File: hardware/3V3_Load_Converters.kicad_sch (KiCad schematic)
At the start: 78 parts, among them J23 61300311121, J24 61300311121, Q28 EPC2016C, Q29 EPC2016C, Q30 EPC2016C, Q31 EPC2016C, Q8 SI2302DDS-T1-GE3, Q9 SI2302DDS-T1-GE3, U21 INA199C3DCKR, U30 LTC3833EUDC-TRPBF, U31 LTC3833EUDC-TRPBF

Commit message: hardware: Making improvements for first release
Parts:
- C10, C11, C20, C21, C3: MPN (none) -> C0603C104K5RACTU; Manufacturer (none) -> KEMET; Package (none) -> SMD 0603; automotive Yes -> (none); automotive grade Grade 1 -> (none); capacitance 0.10 μF -> (none); category Cap -> (none); device class L1 Passive Components -> (none); device class L2 Capacitors -> (none); device class L3 Ceramic Capacitors -> (none); digikey description CAP CER 0.1UF 50V X7R 0603 -> (none); digikey part number 399-5089-2-ND -> (none); height 0.87mm -> (none); lead free Yes -> (none); library id 73022d3323b2b2b8 -> (none); manufacturer KEMET -> (none); material Ceramic -> (none); mouser part number 80-C0603C104K5R7867 -> (none); package 0603 -> (none); rohs Yes -> (none); temperature characteristic X7R -> (none); temperature coefficient 30ppm/°C -> (none); temperature range high +125°C -> (none); temperature range low -55°C -> (none); tolerance 0.1 -> (none); voltage rating 50 V -> (none)
- C12, C13: MPN (none) -> C0603C332J5GACAUTO; Manufacturer (none) -> KEMET; Package (none) -> SMD 0603; automotive Yes -> (none); automotive grade Grade 1 -> (none); capacitance 3,300 pF -> (none); category Cap -> (none); device class L1 Passive Components -> (none); device class L2 Capacitors -> (none); device class L3 Ceramic Capacitors -> (none); digikey description CAP CER 3300PF 50V C0G/NP0 0603 -> (none); digikey part number 399-16013-2-ND -> (none); height 0.87mm -> (none); lead free Yes -> (none); library id bd73e4c017624772 -> (none); manufacturer KEMET -> (none); material Ceramic -> (none); mouser description Cap Ceramic 0.0033uF 50V C0G 5% Pad SMD 0603 125C Automotiv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 -> (none); mouser part number 80-C0603C332J5GAUTO -> (none); package 0603 -> (none); rohs Yes -> (none); temperature characteristic C0G -> (none); temperature coefficient 30ppm/°C -> (none); temperature range high +125°C -> (none); temperature range low -55°C -> (none); tolerance 0.05 -> (none); voltage rating 50 V -> (none)
- C14, C15: MPN (none) -> C0603C101J5GACAUTO; Manufacturer (none) -> KEMET; Package (none) -> SMD 0603; automotive Yes -> (none); automotive grade Grade 1 -> (none); capacitance 100 pF -> (none); category Cap -> (none); device class L1 Passive Components -> (none); device class L2 Capacitors -> (none); device class L3 Ceramic Capacitors -> (none); digikey description CAP CER 100PF 50V C0G/NP0 0603 -> (none); digikey part number 399-6842-2-ND -> (none); height 0.87mm -> (none); lead free Yes -> (none); library id 9466b08f233088f0 -> (none); manufacturer KEMET -> (none); material Ceramic -> (none); mouser description Multilayer Ceramic Capacitors MLCC - SMD/SMT 100pF 50volts 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 -> (none); mouser part number 80-C0603C101J5GAUTO -> (none); package 0603 -> (none); rohs Yes -> (none); temperature characteristic C0G -> (none); temperature coefficient 30ppm/°C -> (none); temperature range high +125°C -> (none); temperature range low -55°C -> (none); tolerance 0.05 -> (none); voltage rating 50 V -> (none)
- C16, C17, C18, C19: MPN (none) -> C0603C102F3GACTU; Manufacturer (none) -> KEMET; Package (none) -> SMD 0603; automotive Yes -> (none); automotive grade Grade 1 -> (none); capacitance 1,000 pF -> (none); category Cap -> (none); device class L1 Passive Components -> (none); device class L2 Capacitors -> (none); device class L3 Ceramic Capacitors -> (none); digikey description CAP CER 1000PF 25V 1% NP0 0603 -> (none); digikey part number C0603C102F3GACTU-ND -> (none); height 0.87mm -> (none); lead free Yes -> (none); library id 46f08c8db7ea7e1d -> (none); manufacturer KEMET -> (none); material Ceramic -> (none); mouser description Capacitor, Ceramic, 1Nf, 25Vdc, 1-% Tol, 1+% Tol, C0g-Tc Co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 -> (none); mouser part number 80-C0603C102F3G -> (none); package 0603 -> (none); rohs Yes -> (none); temperature characteristic C0G -> (none); temperature coefficient 30ppm/°C -> (none); temperature range high +125°C -> (none); temperature range low -55°C -> (none); tolerance 0.01 -> (none); voltage rating 25 V -> (none)
- C22, C23: MPN (none) -> GCM32ER71H475KA55L; Manufacturer (none) -> Murata Electronics; Package (none) -> SMD 1210; automotive Yes -> (none); automotive grade Grade 1 -> (none); capacitance 4.7uF -> (none); category Cap -> (none); device class L1 Passive Components -> (none); device class L2 Capacitors -> (none); device class L3 Ceramic Capacitors -> (none); height 2.7mm -> (none); ipc land pattern name CAPC320250X250 -> (none); lead free Yes -> (none); library id 6d88f107f3aa88d3 -> (none); manufacturer Murata -> (none); material Ceramic -> (none); package 1210 -> (none); rohs Yes -> (none); temperature characteristic X7R -> (none); temperature coefficient 15% -> (none); temperature range high +125°C -> (none); temperature range low -55°C -> (none); tolerance 10% -> (none); voltage rating 50V -> (none)
- C24, C25: MPN (none) -> T495X476K035ATE300; Manufacturer (none) -> KEMET; Package (none) -> SMD 2917; automotive No -> (none); capacitance 47uF -> (none); category Cap -> (none); device class L1 Passive Components -> (none); device class L2 Capacitors -> (none); device class L3 Tantalum Capacitors -> (none); digikey description CAP TANT 47UF 10% 35V 2917 -> (none); digikey part number 399-3905-1-ND -> (none); dissipation factor 8% -> (none); esr 300mΩ -> (none); height 4.3mm -> (none); lead free Yes -> (none); leakage current 16.5uA -> (none); library id 9f2f9997282f5b7d -> (none); life 2000Hours -> (none); manufacturer Kemet -> (none); material Tantalum -> (none); mouser description Tantalum Capacitors - Solid SMD 35volts 47uF 10% ESR=300mOh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 -> (none); mouser part number 80-T495X476K35ATE300 -> (none); package 2917 -> (none); ripple current 742mA -> (none); rohs Yes -> (none); standoff height 0mm -> (none); temperature range high +125°C -> (none); temperature range low -55°C -> (none); tolerance 10% -> (none); voltage rating 35V -> (none)
- C26, C27, C28, C29: MPN (none) -> C1210C106K5RACTU; Manufacturer (none) -> KEMET; Package (none) -> SMD 1210; automotive No -> (none); capacitance 10uF -> (none); category Cap -> (none); device class L1 Passive Components -> (none); device class L2 Capacitors -> (none); device class L3 Ceramic Capacitors -> (none); digikey description CAP CER 10UF 50V X7R 1210 -> (none); digikey part number 399-11629-1-ND -> (none); height 2.8mm -> (none); ipc land pattern name CAPC320250X250 -> (none); lead free Yes -> (none); library id 80b9cd679ce51e4b -> (none); manufacturer KEMET -> (none); material Ceramic -> (none); mouser description Multilayer Ceramic Capacitors MLCC - SMD/SMT 50volts 10uF 1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 -> (none); mouser part number 80-C1210C106K5R -> (none); package 1210 -> (none); rohs Yes -> (none); temperature characteristic X7R -> (none); temperature coefficient 15% -> (none); temperature range high +125°C -> (none); temperature range low -55°C -> (none); tolerance 10% -> (none); voltage rating 50V -> (none)
- C30, C31: MPN (none) -> C0805C105K5RACTU; Manufacturer (none) -> KEMET; Package (none) -> SMD 0805; capacitance 1uF -> (none); category Cap -> (none); device class L1 Passive Components -> (none); device class L2 Capacitors -> (none); device class L3 Ceramic Capacitors -> (none); digikey description CAP CER 1UF 50V X7R 0805 -> (none); digikey part number 399-7409-2-ND -> (none); height 1.4mm -> (none); ipc land pattern name CAPC200125X787 -> (none); lead free yes -> (none); library id ac83af3950e2a3c3 -> (none); manufacturer Kemet -> (none); material Ceramic -> (none); mouser description Multilayer Ceramic Capacitors MLCC - SMD/SMT 1uF 50 Volts 1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 -> (none); mouser part number 80-C0805C105K5R -> (none); package 0805 (2012 metric) -> (none); rohs yes -> (none); standoff height 0mm -> (none); temperature characteristic X7R -> (none); temperature range high +125°C -> (none); temperature range low -55°C -> (none); tolerance 10% -> (none); voltage rating 50V -> (none)
- C32, C33: MPN (none) -> C0603C220K5RACAUTO; Manufacturer (none) -> KEMET; Package (none) -> SMD 0603; automotive Yes -> (none); automotive grade Grade 1 -> (none); capacitance 22 pF -> (none); category Cap -> (none); device class L1 Passive Components -> (none); device class L2 Capacitors -> (none); device class L3 Ceramic Capacitors -> (none); digikey description Cap Ceramic 22pF 50V X7R 10% SMD 0603 125°C Punched Paper T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 -> (none); digikey part number 399-13715-2-ND -> (none); height 0.87mm -> (none); lead free Yes -> (none); library id f369d16140aeee74 -> (none); manufacturer KEMET -> (none); material Ceramic -> (none); mouser description Cap Ceramic 22pF 50V X7R 10% SMD 0603 125°C Punched Paper T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 -> (none); mouser part number 80-C0603C220K5RAUTO -> (none); package 0603 -> (none); rohs Yes -> (none); temperature characteristic X7R -> (none); temperature coefficient 30ppm/°C -> (none); temperature range high +125°C -> (none); temperature range low -55°C -> (none); tolerance 0.1 -> (none); voltage rating 50 V -> (none)
- C34, C35, C36, C37, C38, C39: MPN (none) -> GCM32ER71C226KE19L; Manufacturer (none) -> Murata; Package (none) -> SMD 1210; automotive Yes -> (none); automotive grade Grade 1 -> (none); capacitance 22uF -> (none); category Cap -> (none); device class L1 Passive Components -> (none); device class L2 Capacitors -> (none); device class L3 Ceramic Capacitors -> (none); digikey description Cap Ceramic 22pF 50V X7R 10% SMD 0603 125°C Punched Paper T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 -> (none); digikey part number 399-13715-2-ND -> (none); height 2.7mm -> (none); ipc land pattern name CAPC320250X250 -> (none); lead free Yes -> (none); library id c3f1d06b93fd8ef7 -> (none); manufacturer Murata -> (none); material Ceramic -> (none); mouser description Cap Ceramic 22pF 50V X7R 10% SMD 0603 125°C Punched Paper T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 -> (none); mouser part number 80-C0603C220K5RAUTO -> (none); package 1210 -> (none); rohs Yes -> (none); temperature characteristic X7R -> (none); temperature coefficient 15% -> (none); temperature range high +125°C -> (none); temperature range low -55°C -> (none); tolerance 10% -> (none); voltage rating 16V -> (none)
- JP1, JP2: value SolderJumper_2_Bridged -> N/A; MPN (none) -> N/A; Manufacturer (none) -> N/A; Package (none) -> N/A
- L2: MPN (none) -> 744325240; Manufacturer (none) -> Wurth Elektronik; Manufacturer_Name Wurth Elektronik -> (none); Manufacturer_Part_Number 744325240 -> (none); Mouser Part Number 710-744325240 -> (none); Mouser Price/Stock https://www.mouser.co.uk/ProductDetail/Wurth-Elektronik/744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 -> (none); Package (none) -> Non-standard
- Q28, Q29, Q30, Q31: MPN (none) -> EPC2016C; Manufacturer (none) -> EPC; Package (none) -> Die (specific to EPC2016C); automotive No -> (none); category Trans -> (none); continuous drain current 18A -> (none); depletion mode False -> (none); device class L1 Discrete Semiconductors -> (none); device class L2 Transistors -> (none); device class L3 MOSFETs -> (none); digikey description GANFET TRANS 100V 18A BUMPED DIE -> (none); digikey part number 917-1080-1-ND -> (none); drain to source breakdown voltage 100V -> (none); drain to source resistance 12mΩ -> (none); drain to source voltage 100V -> (none); gate to source voltage +6/-4V -> (none); height 0.815mm -> (none); input capacitace at vds 360pF @ 50V -> (none); lead free Yes -> (none); library id edc307fffab956cd -> (none); manufacturer EPC -> (none); max junction temp +150°C -> (none); number of N channels 1 -> (none); number of channels 1 -> (none); package SMT_2MM106_1MM632 -> (none); pulse drain current 75A -> (none); reverse recovery charge 0nC -> (none); rohs Yes -> (none); rthja max 69°C/W -> (none); standoff height 0.08mm -> (none); technology GaN -> (none); temperature range high +150°C -> (none); temperature range low -40°C -> (none); threshold vgs max 2.5V -> (none); threshold vgs min 0.8V -> (none); typ forward diode voltage 1.8V -> (none)
- Q8, Q9: Height 1.12 -> (none); MPN (none) -> SI2302DDS-T1-GE3; Manufacturer (none) -> Vishay; Manufacturer_Name Vishay -> (none); Manufacturer_Part_Number SI2302DDS-T1-GE3 -> (none); Mouser Part Number 78-SI2302DDS-T1-GE3 -> (none); Mouser Price/Stock https://www.mouser.co.uk/ProductDetail/Vishay-Semiconductor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 -> (none); Package (none) -> SOT-23-3
- R33, R34, R39: Arrow Part Number CRCW0603100KFKEAHP -> (none); Arrow Price/Stock https://www.arrow.com/en/products/crcw0603100kfkeahp/vishay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 -> (none); Height 0.55 -> (none); MPN (none) -> CRCW0603100KFKEAHP; Manufacturer (none) -> Vishay; Manufacturer_Name Vishay -> (none); Manufacturer_Part_Number CRCW0603100KFKEAHP -> (none); Mouser Part Number 71-CRCW0603100KFKEAH -> (none); Mouser Price/Stock https://www.mouser.co.uk/ProductDetail/Vishay-Dale/CRCW0603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 -> (none); Package (none) -> SMD 0603
- R37, R38: MPN (none) -> CRCW060312K0FKEAHP; Manufacturer (none) -> Vishay; Package (none) -> SMD 0603; automotive Yes -> (none); automotive grade Grade 0 -> (none); category Res -> (none); composition Thick Film -> (none); device class L1 Passive Components -> (none); device class L2 Resistors -> (none); device class L3 Chip SMD Resistors -> (none); height 0.55mm -> (none); ipc land pattern name RESC16085X45 -> (none); lead free Yes -> (none); library id e050c09dfdbc8558 -> (none); manufacturer Vishay -> (none); package 0603 -> (none); power 250mW -> (none); power rating 0.33W -> (none); resistance 12kΩ -> (none); rohs Yes -> (none); series CRCW-HP e3 -> (none); temperature coefficient 100ppm/°C -> (none); temperature range high +155°C -> (none); temperature range low -55°C -> (none); tolerance 1% -> (none); voltage rating 75V -> (none)
- R47: MPN (none) -> WSL20108L000FEA18; Manufacturer (none) -> Vishay; Package (none) -> SMD 2010
- R50, R54: MPN (none) -> CRCW060390K9FKEAHP; Manufacturer (none) -> Vishay; Package (none) -> SMD 0603; automotive Yes -> (none); automotive grade Grade 0 -> (none); category Res -> (none); composition Thick Film -> (none); device class L1 Passive Components -> (none); device class L2 Resistors -> (none); device class L3 Chip SMD Resistors -> (none); height 0.55mm -> (none); ipc land pattern name RESC16085X45 -> (none); lead free Yes -> (none); library id 12344a549d2950d0 -> (none); manufacturer Vishay -> (none); package 0603 -> (none); power 250mW -> (none); power rating 0.33W -> (none); resistance 90.9kΩ -> (none); rohs Yes -> (none); series CRCW-HP e3 -> (none); temperature coefficient 100ppm/°C -> (none); temperature range high +155°C -> (none); temperature range low -55°C -> (none); tolerance 1% -> (none); voltage rating 75V -> (none)
- R52, R56: MPN (none) -> CRCW060320K0FKEAHP; Manufacturer (none) -> Vishay; Package (none) -> SMD 0603; automotive Yes -> (none); automotive grade Grade 0 -> (none); category Res -> (none); composition Thick Film -> (none); device class L1 Passive Components -> (none); device class L2 Resistors -> (none); device class L3 Chip SMD Resistors -> (none); height 0.55mm -> (none); ipc land pattern name RESC16085X45 -> (none); lead free Yes -> (none); library id 6d0e00b833a89e4b -> (none); manufacturer Vishay -> (none); package 0603 -> (none); power 250mW -> (none); power rating 0.33W -> (none); resistance 20kΩ -> (none); rohs Yes -> (none); series CRCW-HP e3 -> (none); temperature coefficient 100ppm/°C -> (none); temperature range high +155°C -> (none); temperature range low -55°C -> (none); tolerance 1% -> (none); voltage rating 75V -> (none)
- R76: MPN (none) -> CRCW06030000Z0EAHP; Manufacturer (none) -> Vishay; Package (none) -> SMD 0603
- R97: MPN (none) -> CRCW060382K0FKEA; Manufacturer (none) -> Vishay; Package (none) -> SMD 0603
- TP5: value 3V3 -> Test point; MPN (none) -> N/A; Manufacturer (none) -> N/A; Package (none) -> N/A
- U21: footprint Package_TO_SOT_SMD:SOT-363_SC-70-6 -> footprints:INA199C3DCKR; symbol INA199C3DCKR:INA199xxDCK -> INA199C3DCKR:INA199C3DCKR; MPN (none) -> INA199C3DCKR; Manufacturer (none) -> TI; Package (none) -> SC70-6
- U30, U31: value LTC3833EUDC-TRPBF -> LTC3833EUDC#TRPBF; symbol LTC3833EUDC#TRPBF:LTC3833EUDC-TRPBF -> LTC3833EUDC#TRPBF:LTC3833EUDC#TRPBF; MPN (none) -> LTC3833EUDC#TRPBF; Manufacturer (none) -> Analog Devices; Package (none) -> QFN-20
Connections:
- net AMUX7: no longer U21.6 (OUT)
- net GNDPWR: no longer U21.1 (REF)
- net VBUS_BK3V3: no longer U21.5 (IN-)
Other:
- moved on the sheet: U21

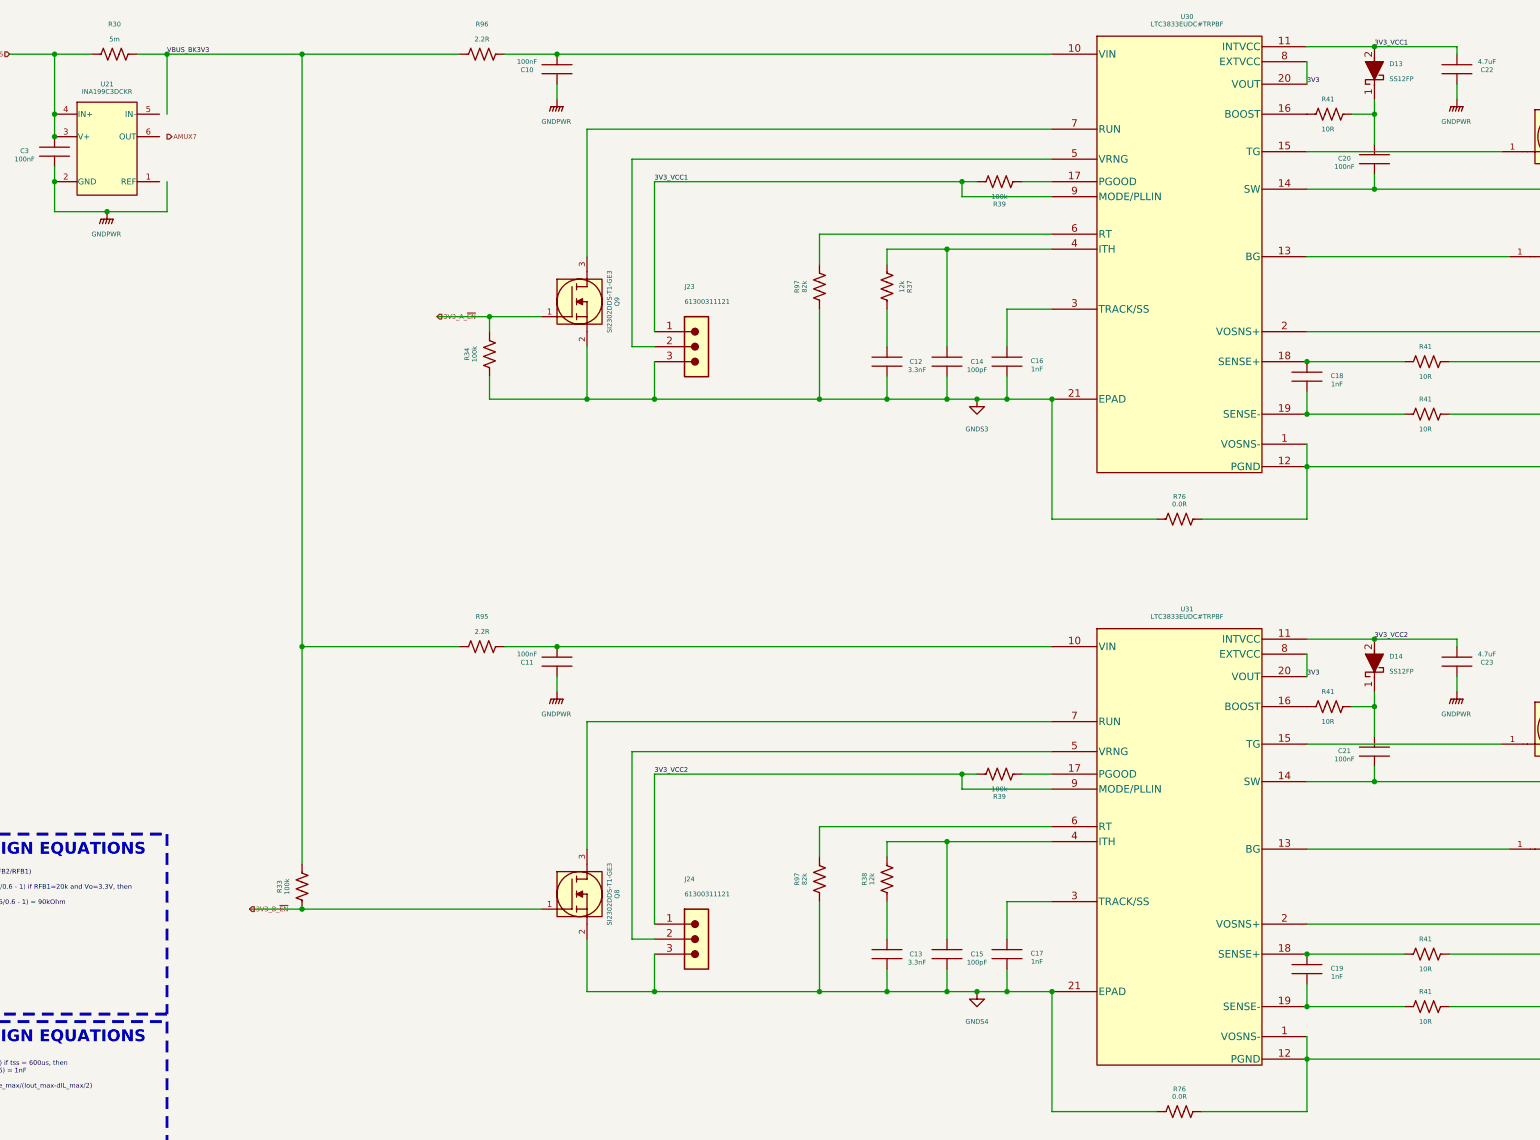
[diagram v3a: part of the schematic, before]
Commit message: hardware: Minor improvements to the schematics
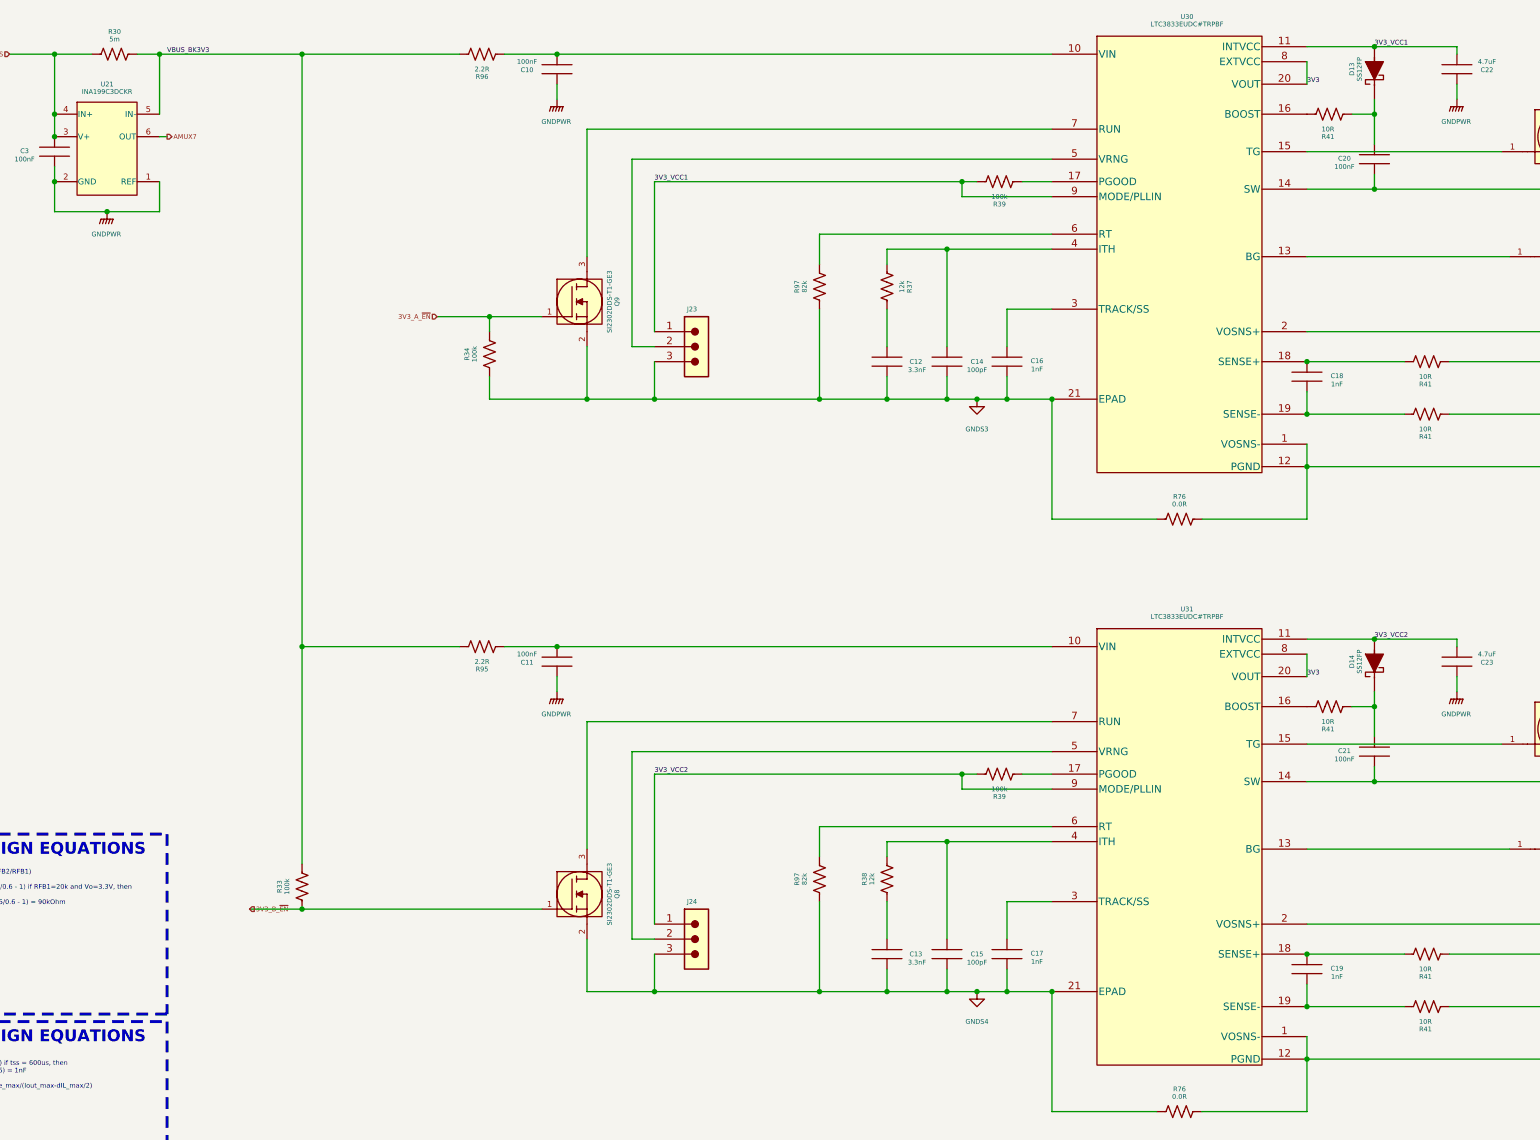
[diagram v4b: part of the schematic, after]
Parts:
- D13, D14: Height 1 -> (none); MPN (none) -> SS12FP; Manufacturer (none) -> onsemi; Manufacturer_Name onsemi -> (none); Manufacturer_Part_Number SS12FP -> (none); Mouser Part Number 512-SS12FP -> (none); Mouser Price/Stock https://www.mouser.co.uk/ProductDetail/ON-Semiconductor-Fai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 -> (none); Package (none) -> SOD-123HE-2
- J23, J24: value 61300311121 -> N/A; symbol 61300311121:61300311121 -> 61300311121:JUMPER_SMD; Height 8.69 -> (none); MPN (none) -> N/A; Manufacturer (none) -> N/A; Manufacturer_Name Wurth Elektronik -> (none); Manufacturer_Part_Number 61300311121 -> (none); Mouser Part Number 710-61300311121 -> (none); Mouser Price/Stock https://www.mouser.co.uk/ProductDetail/Wurth-Elektronik/613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 -> (none); Package (none) -> N/A
- Q28, Q29, Q30, Q31: Package Die (specific to EPC2016C) -> Non-standard
- R30: MPN (none) -> WSL20105L000FEA; Manufacturer (none) -> Vishay; Package (none) -> SMD 2010
- R41: Arrow Part Number CRCW060310R0FKEAHP -> (none); Arrow Price/Stock https://www.arrow.com/en/products/crcw060310r0fkeahp/vishay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 -> (none); Height 0.5 -> (none); MPN (none) -> CRCW060310R0FKEAHP; Manufacturer (none) -> Vishay; Manufacturer_Name Vishay -> (none); Manufacturer_Part_Number CRCW060310R0FKEAHP -> (none); Mouser Part Number 71-CRCW060310R0FKEAH -> (none); Mouser Price/Stock https://www.mouser.co.uk/ProductDetail/Vishay-Dale/CRCW0603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 -> (none); Package (none) -> SMD 0603
- R95, R96: MPN (none) -> CRCW06032R20FKEAHP; Manufacturer (none) -> Vishay; Package (none) -> SMD 0603
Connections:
- net AMUX7: now also U21.6 (OUT)
- net GNDPWR: now also U21.1 (REF)
- net VBUS_BK3V3: now also U21.5 (IN-)

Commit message: hardware: Adding a block diagram of the RE²PS and making minor modifications to the symbols and schematic
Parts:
- J23, J24: symbol 61300311121:JUMPER_SMD -> JUMPER_SMD:JUMPER_SMD; Observations (none) -> The resistor CRCW06030000Z0EAHP (SMD 0603) is connected bet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
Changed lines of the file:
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@@
     )
   )
-  (symbol (lib_id "61300311121:JUMPER_SMD") (at 134.62 72.39 0) (unit 1)
+  (symbol (lib_id "JUMPER_SMD:JUMPER_SMD") (at 134.62 72.39 0) (unit 1)
     (in_bom yes) (on_board yes) (dnp no)
     (property "Reference" "J23" (at 140.97 68.58 0) (do_not_autoplace)
@@
     )
     (property "Package" "N/A" (at 135.89 96.52 0)
+      (effects (font (size 1.27 1.27)) hide)
+    )
+    (property "Observations" "The resistor CRCW06030000Z0EAHP (SMD 0603) is connected between pins 1 and 2" (at 134.62 82.55 0)
       (effects (font (size 1.27 1.27)) hide)
     )
@@
     )
   )
-  (symbol (lib_id "61300311121:JUMPER_SMD") (at 134.62 172.72 0) (unit 1)
+  (symbol (lib_id "JUMPER_SMD:JUMPER_SMD") (at 134.62 172.72 0) (unit 1)
     (in_bom yes) (on_board yes) (dnp no)
     (property "Reference" "J24" (at 140.97 168.91 0) (do_not_autoplace)
@@
       (effects (font (size 1.27 1.27)) hide)
     )
+    (property "Observations" "The resistor CRCW06030000Z0EAHP (SMD 0603) is connected between pins 1 and 2" (at 134.62 182.88 0)
+      (effects (font (size 1.27 1.27)) hide)
+    )

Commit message: hardware: Minor modifications for the upcoming release
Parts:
- TP5: MPN N/A -> S2761-46R; Manufacturer N/A -> Harwin; Package N/A -> Non-standard
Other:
- moved on the sheet: C30, C31
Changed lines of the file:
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@@
     (stroke (width 0) (type default))
   )
-  (wire (pts (xy 346.71 121.92) (xy 354.33 121.92))
+  (wire (pts (xy 346.71 121.92) (xy 356.87 121.92))
     (stroke (width 0.5) (type default))
   )
@@
     (stroke (width 0) (type default))
   )
-  (wire (pts (xy 346.71 129.54) (xy 354.33 129.54))
+  (wire (pts (xy 346.71 129.54) (xy 356.87 129.54))
     (stroke (width 0) (type default))
   )
@@
     (stroke (width 0) (type default))
   )
-  (wire (pts (xy 346.71 29.21) (xy 354.33 29.21))
+  (wire (pts (xy 346.71 29.21) (xy 356.87 29.21))
     (stroke (width 0) (type default))
   )
@@
     (stroke (width 0.5) (type default))
   )
-  (wire (pts (xy 346.71 21.59) (xy 354.33 21.59))
+  (wire (pts (xy 346.71 21.59) (xy 356.87 21.59))
     (stroke (width 0.5) (type default))
   )
@@
     (stroke (width 0) (type default))
   )
-  (wire (pts (xy 354.33 127) (xy 354.33 129.54))
+  (wire (pts (xy 356.87 127) (xy 356.87 129.54))
     (stroke (width 0) (type default))
   )
@@
     (stroke (width 0) (type default))
   )
-  (wire (pts (xy 354.33 26.67) (xy 354.33 29.21))
+  (wire (pts (xy 356.87 26.67) (xy 356.87 29.21))
     (stroke (width 0) (type default))
   )
@@
       (effects (font (size 1.27 1.27)) hide)
     )
-    (property "Datasheet" "N/A" (at 266.7 270.51 0)
+    (property "Datasheet" "https://br.mouser.com/datasheet/2/181/S2761R-1291319.pdf" (at 266.7 270.51 0)
       (effects (font (size 1.27 1.27)) hide)
     )
-    (property "MPN" "N/A" (at 269.24 270.51 0)
+    (property "MPN" "S2761-46R" (at 269.24 270.51 0)
       (effects (font (size 1.27 1.27)) hide)
     )
-    (property "Package" "N/A" (at 271.78 270.51 0)
+    (property "Package" "Non-standard" (at 271.78 270.51 0)
       (effects (font (size 1.27 1.27)) hide)
     )
-    (property "Manufacturer" "N/A" (at 274.32 270.51 0)
+    (property "Manufacturer" "Harwin" (at 274.32 270.51 0)
       (effects (font (size 1.27 1.27)) hide)
     )
@@
     )
   )
-  (symbol (lib_id "C0805C105K5RACTU:C0805C105K5RACTU") (at 354.33 121.92 0) (unit 1)
+  (symbol (lib_id "C0805C105K5RACTU:C0805C105K5RACTU") (at 356.87 121.92 0) (unit 1)
     (in_bom yes) (on_board yes) (dnp no)
-    (property "Reference" "C31" (at 359.41 124.333 0) (do_not_autoplace)
+    (property "Reference" "C31" (at 361.95 124.333 0) (do_not_autoplace)
       (effects (font (size 0.8 0.8)))
     )
-    (property "Value" "1uF" (at 359.41 125.73 0) (do_not_autoplace)
+    (property "Value" "1uF" (at 361.95 125.73 0) (do_not_autoplace)
       (effects (font (size 0.8 0.8)))
     )
-    (property "Footprint" "footprints:C0805C105K5RACTU" (at 337.82 140.97 0)
+    (property "Footprint" "footprints:C0805C105K5RACTU" (at 340.36 140.97 0)
       (effects (font (size 1.27 1.27)) (justify left) hide)
     )
-    (property "Datasheet" "http://www.kemet.com/Lists/ProductCatalog/Attachments/53/KEM_C1002_X7R_SMD.pdf" (at 337.82 138.43 0)
+    (property "Datasheet" "http://www.kemet.com/Lists/ProductCatalog/Attachments/53/KEM_C1002_X7R_SMD.pdf" (at 340.36 138.43 0)
       (effects (font (size 1.27 1.27)) (justify left) hide)
     )
-    (property "Package" "SMD 0805" (at 350.52 144.78 0)
+    (property "Package" "SMD 0805" (at 353.06 144.78 0)
       (effects (font (size 1.27 1.27)) (justify left) hide)
     )
-    (property "Manufacturer" "KEMET" (at 355.6 135.89 0)
+    (property "Manufacturer" "KEMET" (at 358.14 135.89 0)
       (effects (font (size 1.27 1.27)) hide)
     )
-    (property "MPN" "C0805C105K5RACTU" (at 355.6 133.35 0)
+    (property "MPN" "C0805C105K5RACTU" (at 358.14 133.35 0)
       (effects (font (size 1.27 1.27)) hide)
     )
@@
     )
   )
-  (symbol (lib_id "C0805C105K5RACTU:C0805C105K5RACTU") (at 354.33 21.59 0) (unit 1)
+  (symbol (lib_id "C0805C105K5RACTU:C0805C105K5RACTU") (at 356.87 21.59 0) (unit 1)
     (in_bom yes) (on_board yes) (dnp no)
-    (property "Reference" "C30" (at 359.41 24.003 0) (do_not_autoplace)
+    (property "Reference" "C30" (at 361.95 24.003 0) (do_not_autoplace)
       (effects (font (size 0.8 0.8)))
     )
-    (property "Value" "1uF" (at 359.41 25.4 0) (do_not_autoplace)
+    (property "Value" "1uF" (at 361.95 25.4 0) (do_not_autoplace)
       (effects (font (size 0.8 0.8)))
     )
-    (property "Footprint" "footprints:C0805C105K5RACTU" (at 337.82 40.64 0)
+    (property "Footprint" "footprints:C0805C105K5RACTU" (at 340.36 40.64 0)
       (effects (font (size 1.27 1.27)) (justify left) hide)
     )
-    (property "Datasheet" "http://www.kemet.com/Lists/ProductCatalog/Attachments/53/KEM_C1002_X7R_SMD.pdf" (at 337.82 38.1 0)
+    (property "Datasheet" "http://www.kemet.com/Lists/ProductCatalog/Attachments/53/KEM_C1002_X7R_SMD.pdf" (at 340.36 38.1 0)
       (effects (font (size 1.27 1.27)) (justify left) hide)
     )
-    (property "Package" "SMD 0805" (at 350.52 44.45 0)
+    (property "Package" "SMD 0805" (at 353.06 44.45 0)
       (effects (font (size 1.27 1.27)) (justify left) hide)
     )
-    (property "Manufacturer" "KEMET" (at 355.6 35.56 0)
+    (property "Manufacturer" "KEMET" (at 358.14 35.56 0)
       (effects (font (size 1.27 1.27)) hide)
     )
-    (property "MPN" "C0805C105K5RACTU" (at 355.6 33.02 0)
+    (property "MPN" "C0805C105K5RACTU" (at 358.14 33.02 0)
       (effects (font (size 1.27 1.27)) hide)
     )

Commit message: hardware: update schematic and layout projects
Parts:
- R80, R81, R82, R84, RGND3, RGND4: renamed from R76; value 0.0R -> 0R
- renumbered C12 to C100, C13 to C101, C14 to C102, C15 to C103, C16 to C104, C17 to C105, C18 to C106, C19 to C107, C20 to C108, C21 to C109, C22 to C110, C23 to C111, C24 to C112, C25 to C113, C26 to C114, C27 to C115, C28 to C116, C29 to C117, C30 to C118, C31 to C119, C32 to C120, C33 to C121, C34 to C122, C35 to C123, C36 to C124, C37 to C125, C38 to C126, C39 to C127, C3 to C40, C10 to C98, C11 to C99, JP1 to JP3, JP2 to JP4, L2 to L4, L2 to L8, R34 to R123, R33 to R124, R37 to R127, R38 to R128, R50 to R140, R52 to R142, R54 to R144, R56 to R146, R30 to R29, R41 to R61, R41 to R62, R41 to R63, R41 to R64, R41 to R65, R41 to R66, R39 to R73, R39 to R74, R47 to R78, R47 to R79, R97 to R98
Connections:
- net GNDPWR: now also C112.2, C113.2; no longer C112.1 (CATHODE), C113.1 (CATHODE)
- net VBUS_BK3V3: now also C112.1, C113.1; no longer C112.2 (ANODE), C113.2 (ANODE)
